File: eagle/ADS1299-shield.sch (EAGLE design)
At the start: 118 parts, among them IC1 24AA256UID, IC2 TPS72325DBVT, IC3 TPS73225DBVT, J8 Electrode Connector, U1 ADS1299IPAG, U2 TXB0108PWR, U3 TXB0108PWR

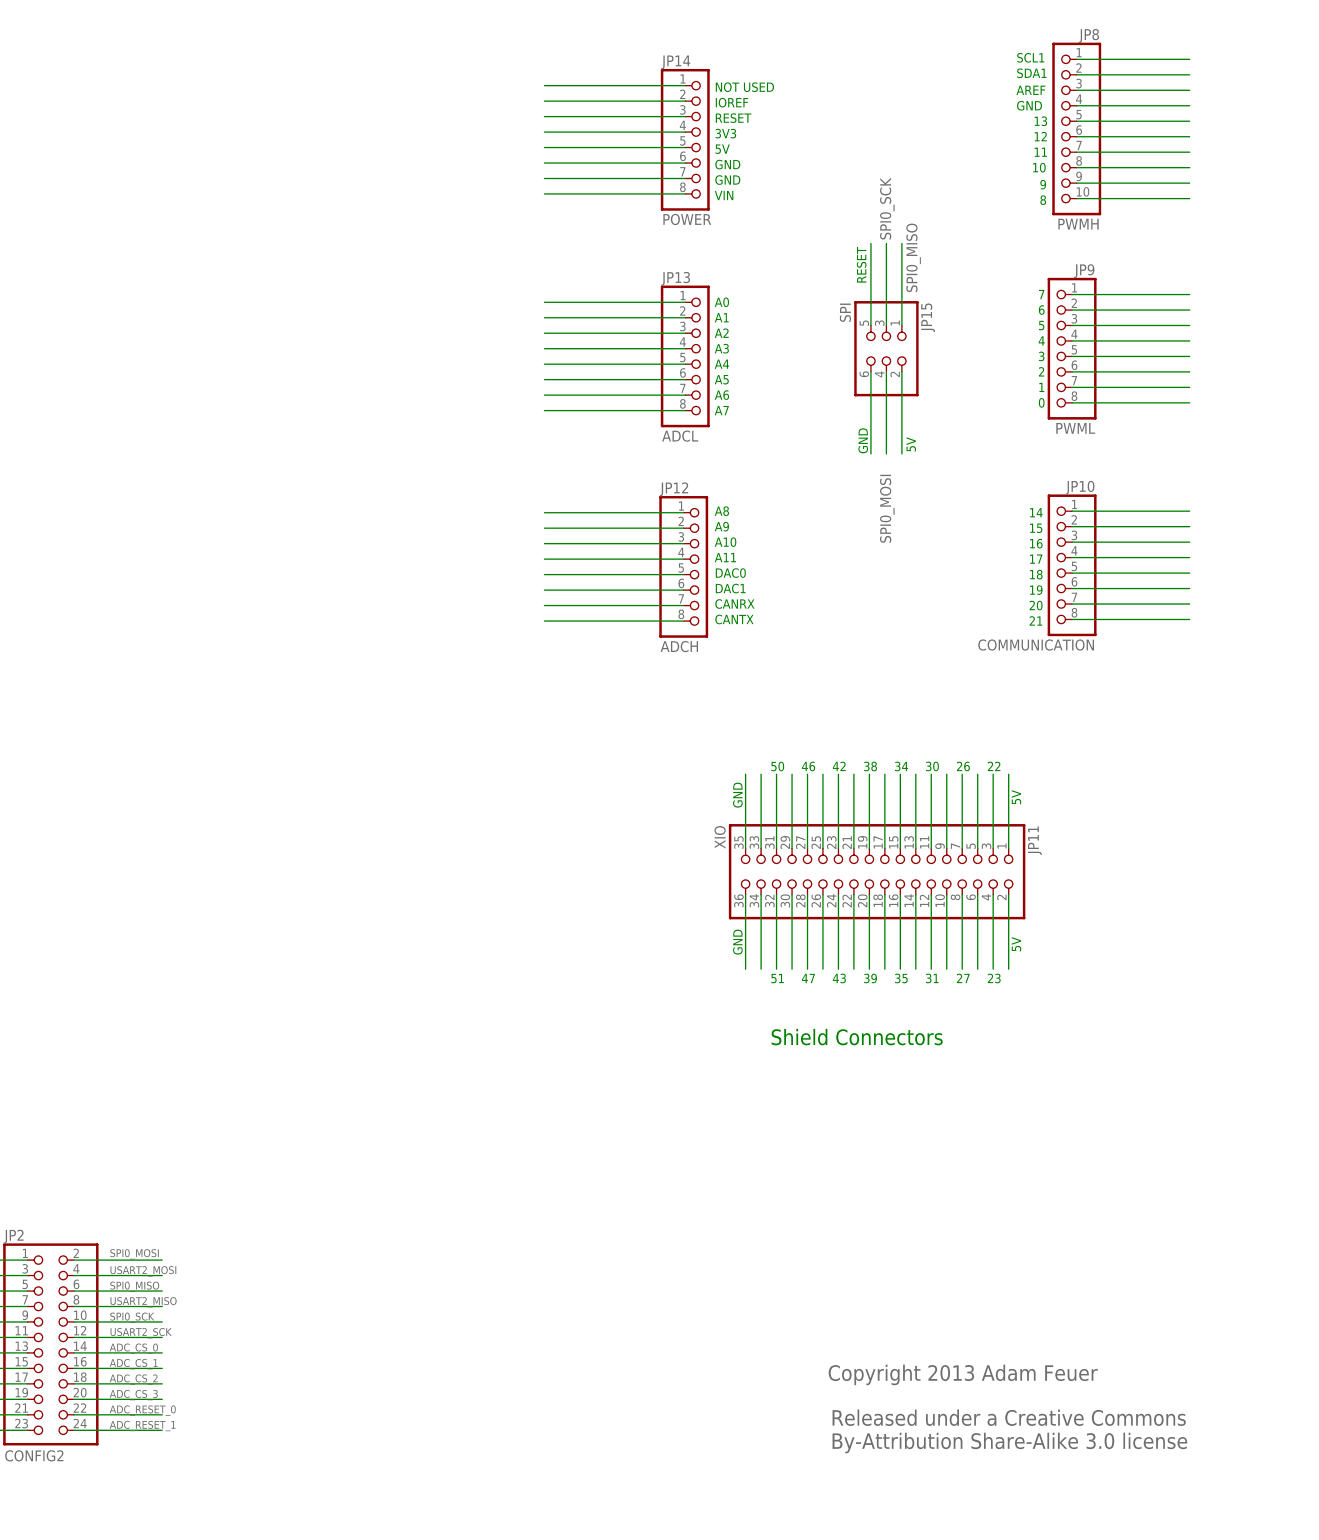
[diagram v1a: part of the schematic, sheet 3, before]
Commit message: added connections for ADC SPI IN, OUT, CLK; and ADC_CLK
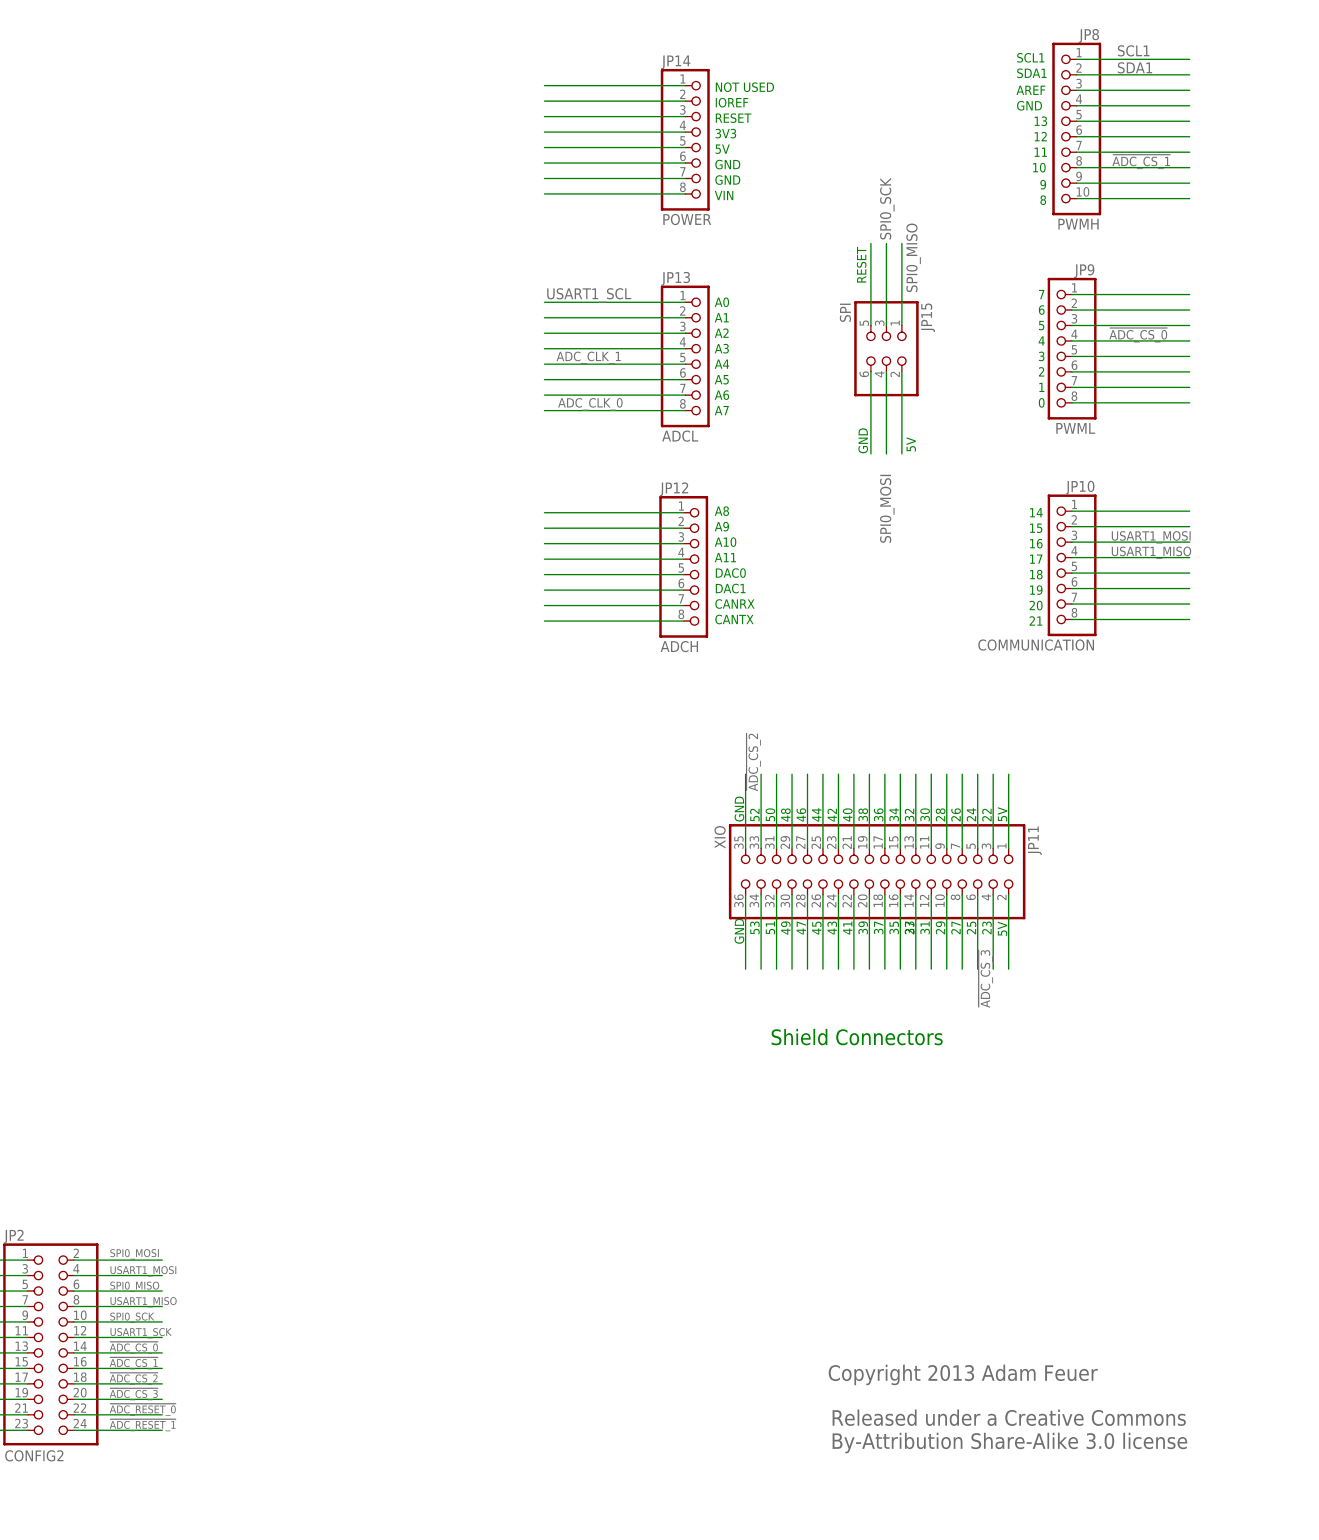
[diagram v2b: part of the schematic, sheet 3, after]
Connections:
- net N$22 renamed USART1_SCL
- net USART2_SCK renamed USART1_SCK
- removed net ADC_CS_0: JP2.14
- removed net ADC_CS_1: JP2.16
- removed net ADC_CS_2: JP2.18
- removed net ADC_CS_3: JP2.20
- removed net ADC_RESET_0: JP2.22
- removed net ADC_RESET_1: JP2.24
- removed net N$112: JP11.33
- removed net N$25: JP8.1
- removed net N$26: JP8.2
- removed net N$32: JP8.8
- removed net N$37: JP9.4
- removed net N$43: JP10.3
- removed net N$44: JP10.4
- removed net N$55: JP13.8
- removed net N$56: JP13.7
- removed net N$58: JP13.5
- removed net N$93: JP11.4
- removed net USART2_MISO: JP2.8
- removed net USART2_MOSI: JP2.4
- new net !ADC_CS_0: JP2.14, JP9.4
- new net !ADC_CS_1: JP2.16, JP8.8
- new net !ADC_CS_2: JP11.33, JP2.18
- new net !ADC_CS_3: JP11.4, JP2.20
- new net USART1_MISO: JP10.4, JP2.8
- new net USART1_MOSI: JP10.3, JP2.4
- net !ADC_RESET_0: now also JP2.22
- net !ADC_RESET_1: now also JP2.24
- net ADC_CLK_0: now also JP13.7, JP13.8
- net ADC_CLK_1: now also JP13.5
- net SCL1: now also JP8.1
- net SDA1: now also JP8.2
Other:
- note added: "24"
- note added: "25"
- note added: "28"
- note added: "29"
- note added: "32"
- note added: "33"
- note added: "36"
- note added: "37"
- note added: "40"
- note added: "41"
- note added: "44"
- note added: "45"
- note added: "48"
- note added: "49"
- note added: "52"
- note added: "53"

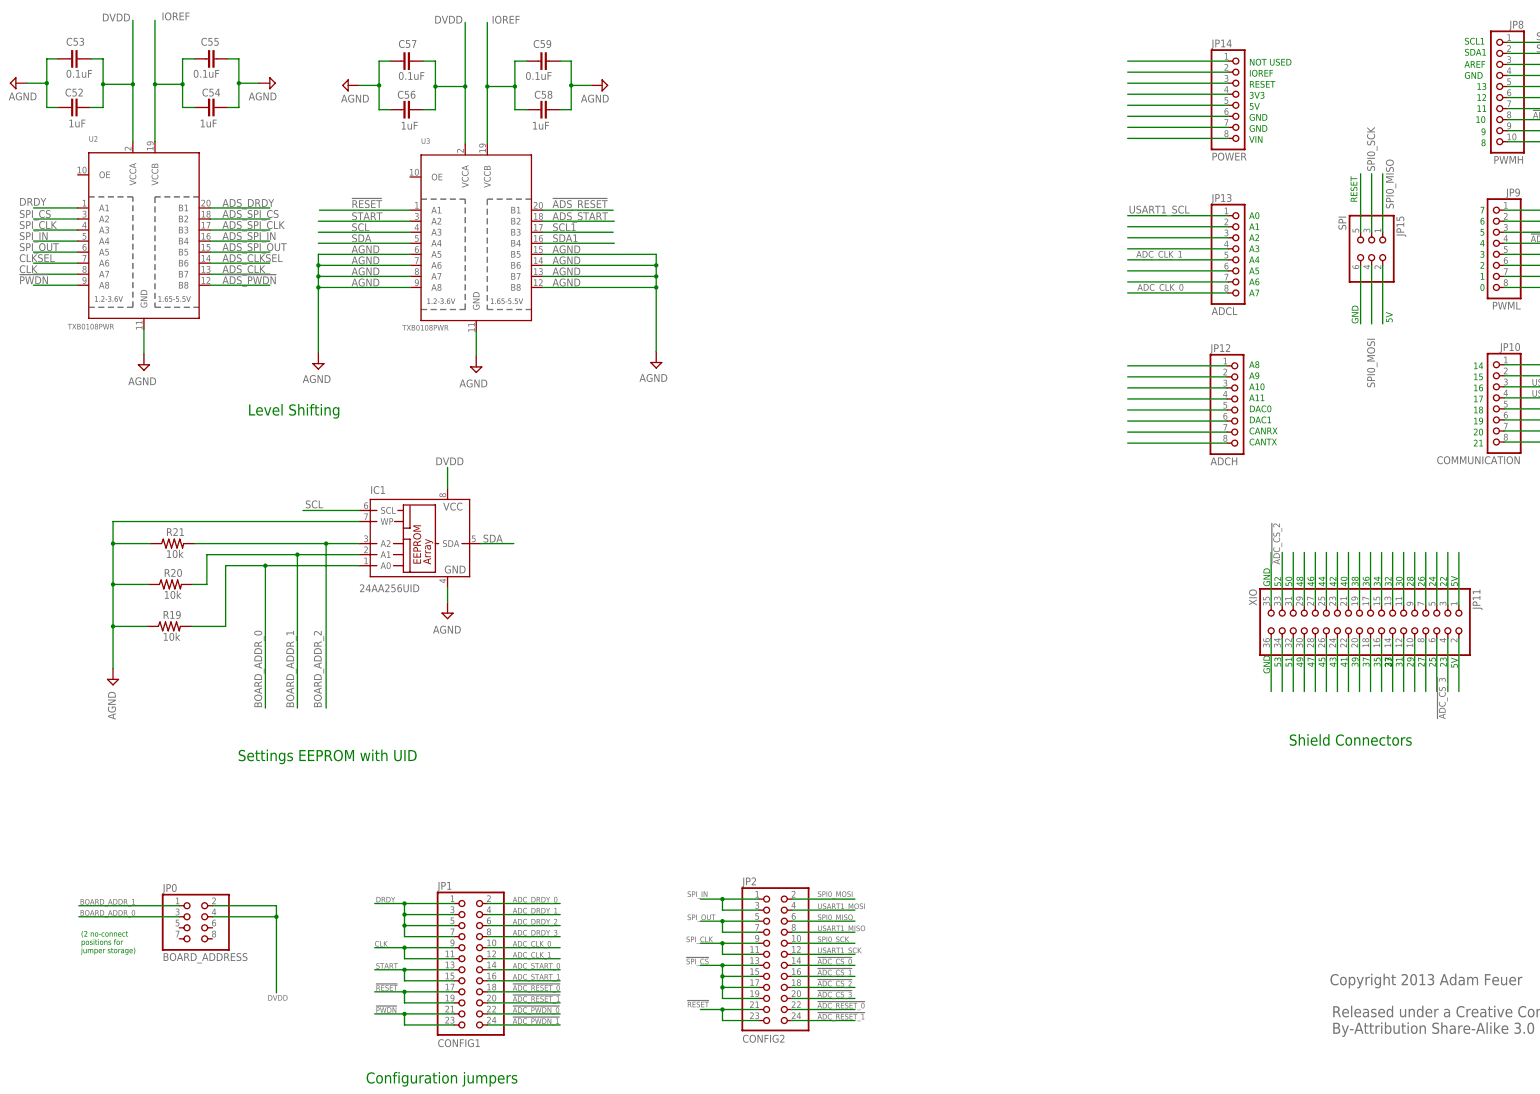
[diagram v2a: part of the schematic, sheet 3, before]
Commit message: all necessary signals routed to shield connectors; schematic passes ERC
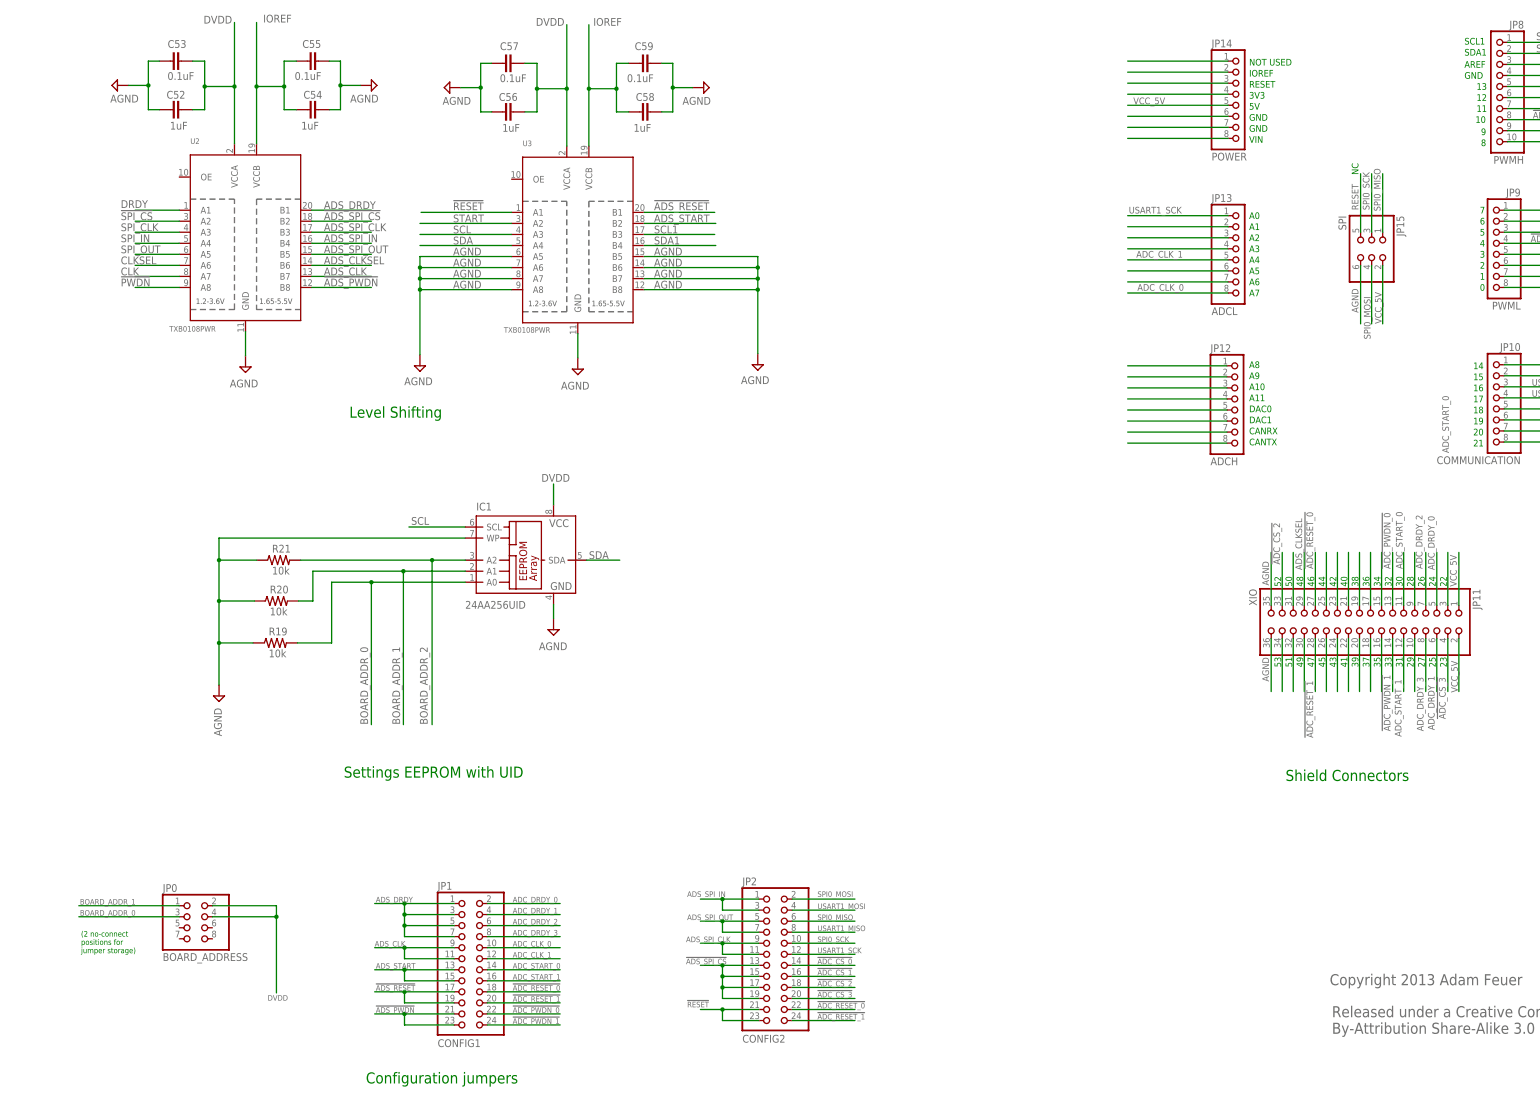
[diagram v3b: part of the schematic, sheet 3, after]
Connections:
- removed net 5V: JP15.2
- removed net ADS_SPI_CS: U2.B2
- removed net BIASREF: U1.BIASREF
- removed net DAISY_IN: U1.DAISY_IN
- removed net N$100: JP11.13
- removed net N$109: JP11.27
- removed net N$110: JP11.29
- removed net N$65: JP14.5
- removed net N$75: JP11.35
- removed net N$76: JP11.2
- removed net N$77: JP11.36
- removed net N$81: JP11.28
- removed net N$88: JP11.14
- removed net N$89: JP11.12
- removed net N$91: JP11.8
- removed net N$92: JP11.6
- removed net N$94: JP11.1
- removed net N$96: JP11.5
- removed net N$97: JP11.7
- removed net N$99: JP11.11
- removed net SPI_CS: U2.A2
- removed net USART1_SCL: JP13.1
- new net !ADS_SPI_CS: JP2.13, JP2.15, JP2.17, JP2.19, U2.B2
- new net N$501: JP13.7
- net !ADC_PWDN_0: now also JP11.13
- net !ADC_PWDN_1: now also JP11.14
- net !ADC_RESET_0: now also JP11.27
- net !ADC_RESET_1: now also JP11.28
- net !ADS_PWDN: now also JP1.21, JP1.23
- net !ADS_RESET: now also JP1.17, JP1.19
- net !PWDN: no longer JP1.21, JP1.23
- net !RESET: no longer JP1.17, JP1.19
- net !SPI_CS: now also U2.A2; no longer JP2.13, JP2.15, JP2.17, JP2.19
- net ADC_CLK_0: no longer JP13.7
- net ADC_DRDY_0: now also JP11.5
- net ADC_DRDY_1: now also JP11.6
- net ADC_DRDY_2: now also JP11.7
- net ADC_DRDY_3: now also JP11.8
- net ADC_START_0: now also JP11.11
- net ADC_START_1: now also JP11.12
- net ADS_CLK: now also JP1.11, JP1.9
- net ADS_CLKSEL: now also JP11.29
- net ADS_DRDY: now also JP1.1, JP1.3, JP1.5, JP1.7
- net ADS_SPI_CLK: now also JP2.11, JP2.9
- net ADS_SPI_IN: now also JP2.1, JP2.3
- net ADS_SPI_OUT: now also JP2.5, JP2.7
- net ADS_START: now also JP1.13, JP1.15
- net AGND: now also JP11.35, JP11.36, JP15.6, U1.DAISY_IN
- net CLK: no longer JP1.11, JP1.9
- net DRDY: no longer JP1.1, JP1.3, JP1.5, JP1.7
- net GND: no longer JP15.6
- net SPI_CLK: no longer JP2.11, JP2.9
- net SPI_IN: no longer JP2.1, JP2.3
- net SPI_OUT: no longer JP2.5, JP2.7
- net START: no longer JP1.13, JP1.15
- net USART1_SCK: now also JP13.1
- net VCC_5V: now also JP11.1, JP11.2, JP14.5, JP15.2
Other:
- moved on the sheet: C52, C53, C54, C55, C56, C57, C58, C59, IC1, R19, R20, R21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
